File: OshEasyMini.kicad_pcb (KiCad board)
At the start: 6 copper layers, 17.2 x 35.4 mm, 120 parts, among them J1 TAGCONNECT, J10 Conn_01x04_MountingPin, J3 SMA_Edgelaunch, J4 PYROS, J5 UFL, J6 BAT, Q1 SiA449DJ, Q2 AO3400A, Q3 SiA449DJ, U1 MIA-M10Q, U11 CPT-7502-65-SMT-TR, U12 LM293QT, U17 MCP73831-2-OT, U18 TC2185-3.3VxCTTR, U19 W25Q64JVXGIQ, U2 WE-TVS-82400102, U20 SISB46DN, U21 SN74LVC1G80QDCKTQ1, U3 ADXL375, U4 MS5607-02BA, U6 MCP130-xxxxTT, U7 DRV5012AEDMRR, U8 CC1200, U9 ATSAMD21G17D-A, X2 ECS-160-8-36Q-AES-TR1, Y1 40mhz 8pF 30 Ohms, Y2 32.768khz

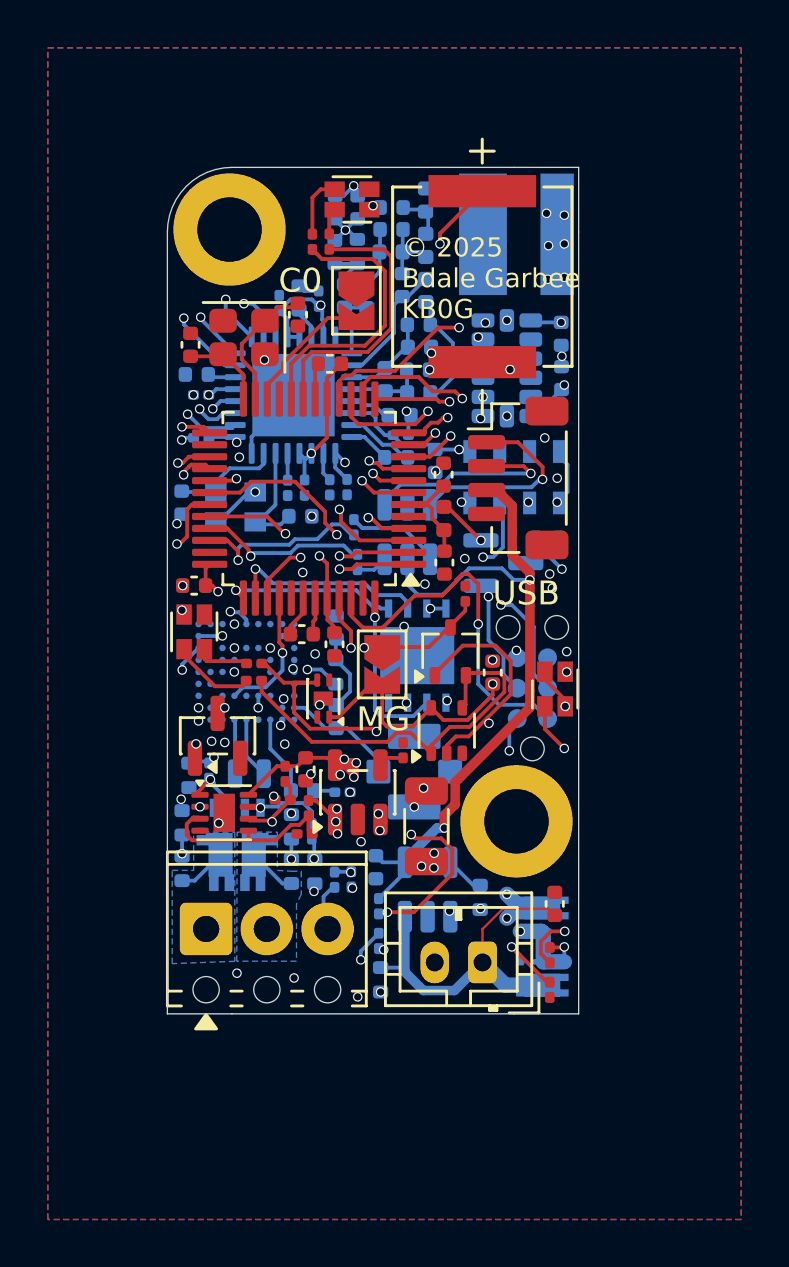
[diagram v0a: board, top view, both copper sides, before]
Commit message: CRITICAL: GPS UART RX/TX swapped. Fixed.
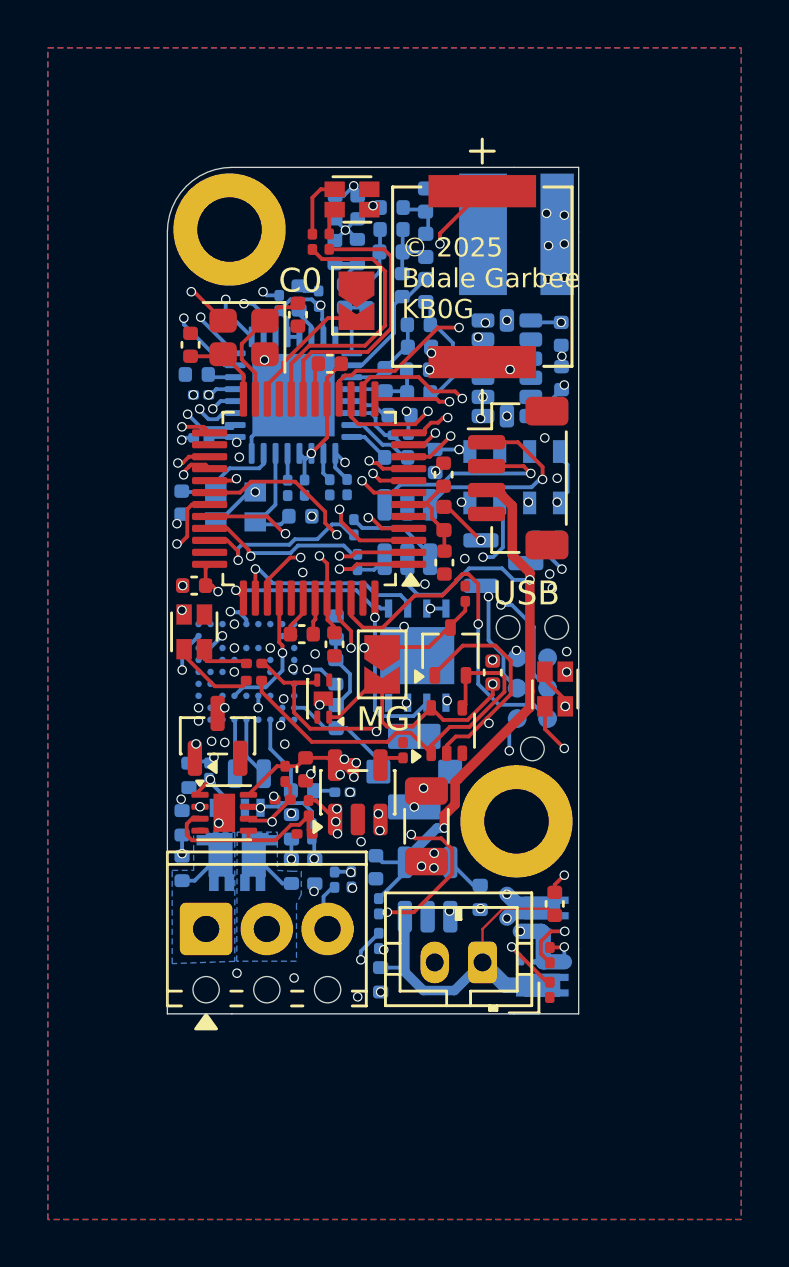
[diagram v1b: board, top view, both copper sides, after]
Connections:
- H1 pad 1: GND -> unconnected-(H1-Pad1)
- H2 pad 1: GND -> unconnected-(H2-Pad1)
- J3 pad 1: GND -> Net-(J3-In)
- U1 pad G1: /TX1 -> /RX1
- U1 pad H1: /RX1 -> /TX1
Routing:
- net Net-(J3-In): track 2.31 -> 4.23 mm, vias 0 -> 6
- net GND: track 16.9 -> 18.4 mm, vias 59 -> 56
- net /TX1: track 12.5 -> 13.0 mm

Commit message: fixed gnd pad for antenna. Also investigating rf frontend capacitor types
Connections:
- J3 pad 1: Net-(J3-In) -> GND
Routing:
- net Net-(J3-In): track 4.23 -> 2.31 mm, vias 6 -> 0
- net GND: track 18.4 -> 20.3 mm, vias 56 -> 62
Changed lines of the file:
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@@
 	)
 	(footprint "Connector_Coaxial:SMA_Amphenol_132289_EdgeMount"
+		(locked yes)
 		(layer "B.Cu")
 		(at 103.2 32.8 90)
@@
 	)
 	(footprint "Connector_Coaxial:SMA_Amphenol_132289_EdgeMount"
+		(locked yes)
 		(layer "B.Cu")
 		(at 106.3 32.8 90)
@@
 		(sheetname "/")
 		(sheetfile "OshEasyMini.kicad_sch")
-		(attr smd exclude_from_pos_files)
+		(attr smd board_only exclude_from_pos_files)
 		(fp_line
 			(start 3.54 0)
@@
 		)
 		(pad "1" smd rect
-			(at 0 0 180)
+			(at 0 0)
 			(size 1.4 5.08)
 			(layers "B.Cu" "B.Mask")
-			(net 26 "Net-(J3-In)")
+			(net 1 "GND")
 			(pinfunction "In")
 			(pintype "passive")
@@
 	)
 	(via
+		(at 105.856124 31.919948)
+		(size 0.4)
+		(drill 0.3)
+		(layers "F.Cu" "B.Cu")
+		(net 1)
+	)
+	(via
+		(at 105.941802 33.273649)
+		(size 0.4)
+		(drill 0.3)
+		(layers "F.Cu" "B.Cu")
+		(net 1)
+	)
+	(via
 		(at 90.4 44.9)
 		(size 0.4)
@@
 	)
 	(via
+		(at 106.6 34.6)
+		(size 0.4)
+		(drill 0.3)
+		(layers "F.Cu" "B.Cu")
+		(net 1)
+	)
+	(via
 		(at 92.15 57.425)
 		(size 0.4)
@@
 	)
 	(via
+		(at 106.6 32)
+		(size 0.4)
+		(drill 0.3)
+		(layers "F.Cu" "B.Cu")
+		(net 1)
+	)
+	(via
 		(at 94 35.2)
 		(size 0.4)
@@
 	)
 	(via
+		(at 105.907531 34.678756)
+		(size 0.4)
+		(drill 0.3)
+		(layers "F.Cu" "B.Cu")
+		(net 1)
+	)
+	(via
+		(at 106.6 33.2)
+		(size 0.4)
+		(drill 0.3)
+		(layers "F.Cu" "B.Cu")
+		(net 1)
+	)
+	(via
 		(at 101.041826 37.772156)
 		(size 0.4)
@@
 	)
 	(segment
+		(start 105.907531 34.492469)
+		(end 106 34.4)
+		(width 0.1)
+		(layer "B.Cu")
+		(net 1)
+	)
+	(segment
 		(start 106.470391 37.443131)
 		(end 106.470391 37.870391)
@@
 	)
 	(segment
+		(start 106 34.4)
+		(end 106 32.8)
+		(width 0.1)
+		(layer "B.Cu")
+		(net 1)
+	)
+	(segment
 		(start 94.677814 35.353629)
 		(end 94.153629 35.353629)
@@
 	)
 	(segment
+		(start 105.907531 34.678756)
+		(end 105.907531 34.492469)
+		(width 0.1)
+		(layer "B.Cu")
+		(net 1)
+	)
+	(segment
 		(start 98.84 62.67)
 		(end 99 62.67)
@@
 		(net 25)
 	)
-	(via
-		(at 105.856124 31.919948)
-		(size 0.4)
-		(drill 0.3)
-		(layers "F.Cu" "B.Cu")
-		(net 26)
-	)
-	(via
-		(at 105.941802 33.273649)
-		(size 0.4)
-		(drill 0.3)
-		(layers "F.Cu" "B.Cu")
-		(net 26)
-	)
-	(via
-		(at 106.6 34.6)
-		(size 0.4)
-		(drill 0.3)
-		(layers "F.Cu" "B.Cu")
-		(net 26)
-	)
-	(via
-		(at 106.6 32)
-		(size 0.4)
-		(drill 0.3)
-		(layers "F.Cu" "B.Cu")
-		(net 26)
-	)
-	(via
-		(at 105.907531 34.678756)
-		(size 0.4)
-		(drill 0.3)
-		(layers "F.Cu" "B.Cu")
-		(net 26)
-	)
-	(via
-		(at 106.6 33.2)
-		(size 0.4)
-		(drill 0.3)
-		(layers "F.Cu" "B.Cu")
-		(net 26)
-	)
-	(segment
-		(start 105.907531 34.492469)
-		(end 106 34.4)
-		(width 0.1)
-		(layer "B.Cu")
-		(net 26)
-	)
 	(segment
 		(start 103.108791 30.881209)
@@
 		(layer "B.Cu")
 		(net 26)
-	)
-	(segment
-		(start 106 34.4)
-		(end 106 32.8)
-		(width 0.1)
-		(layer "B.Cu")
-		(net 26)
-	)
-	(segment
-		(start 105.907531 34.678756)
-		(end 105.907531 34.492469)
-		(width 0.1)
-		(layer "B.Cu")
-		(net 26)
